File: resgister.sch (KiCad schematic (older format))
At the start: 8 parts, among them U1 74LS245, U2 74LS173, U3 74LS173, U4 74LS245, U5 74LS173, U6 74LS173

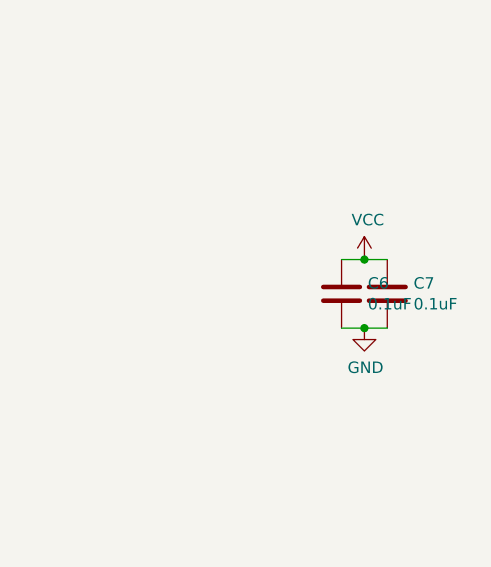
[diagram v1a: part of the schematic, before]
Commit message: added display
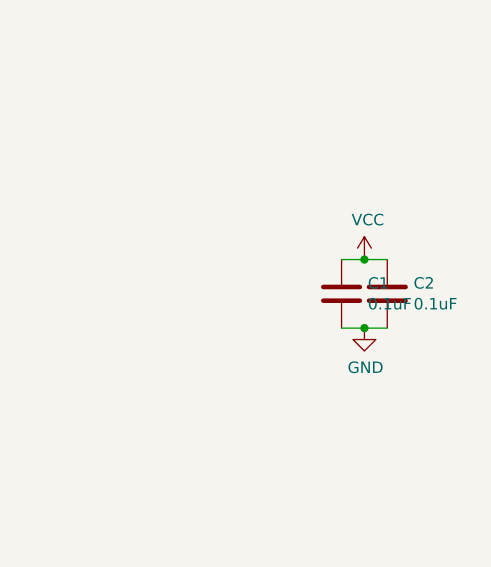
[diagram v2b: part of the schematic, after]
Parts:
- renumbered C8 to C3, C9 to C4

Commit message: clean up
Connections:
- wire segments 281 -> 262
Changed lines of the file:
@@
 $Descr A3 16535 11693
 encoding utf-8
-Sheet 2 23
+Sheet 4 23
 Title ""
 Date ""
@@
 Wire Wire Line
 	3800 4350 3800 1150
-Connection ~ 3800 1150
-Connection ~ 3900 1050
-Connection ~ 4000 950
-Connection ~ 4100 850
-Wire Wire Line
-	3900 1050 9850 1050
-Wire Wire Line
-	3800 1150 9850 1150
-Wire Wire Line
-	4000 950  9850 950
-Wire Wire Line
-	4100 850  9850 850
 Wire Wire Line
 	2000 6100 3250 6100
@@
 Wire Wire Line
 	2700 4100 5250 4100
-Connection ~ 5350 1550
-Connection ~ 5450 1450
-Connection ~ 5550 1350
-Connection ~ 5650 1250
-Wire Wire Line
-	5650 1250 9850 1250
-Wire Wire Line
-	5550 1350 9850 1350
-Wire Wire Line
-	5450 1450 9850 1450
-Wire Wire Line
-	5350 1550 9850 1550
 Wire Wire Line
 	1300 1750 6200 1750
@@
 Wire Wire Line
 	6800 2350 9450 2350
-Connection ~ 7900 1950
-Wire Wire Line
-	7900 1950 9850 1950
-Connection ~ 8000 1850
-Wire Wire Line
-	8000 1850 9850 1850
-Connection ~ 8100 1750
-Wire Wire Line
-	8100 1750 9850 1750
-Connection ~ 8200 1650
-Wire Wire Line
-	8200 1650 9850 1650
-Connection ~ 9450 2350
-Wire Wire Line
-	9450 2350 9850 2350
-Connection ~ 9550 2250
-Wire Wire Line
-	9550 2250 9850 2250
-Connection ~ 9650 2150
-Wire Wire Line
-	9650 2150 9850 2150
-Connection ~ 9750 2050
-Wire Wire Line
-	9750 2050 9850 2050
 Wire Wire Line
 	6100 6900 7500 6900
@@
 AR Path="/5FB94562/61968D37" Ref="#PWR?"  Part="1"
 AR Path="/616D5CDC/61968D37" Ref="#PWR?"  Part="1"
-F 0 "#PWR02" H 2600 4600 50  0001 C CNN
+F 0 "#PWR024" H 2600 4600 50  0001 C CNN
 F 1 "GND" H 2605 4677 50  0000 C CNN
 F 2 "" H 2600 4850 50  0001 C CNN
@@
 AR Path="/5FB94562/61968D38" Ref="#PWR?"  Part="1"
 AR Path="/616D5CDC/61968D38" Ref="#PWR?"  Part="1"
-F 0 "#PWR03" H 3300 3250 50  0001 C CNN
+F 0 "#PWR025" H 3300 3250 50  0001 C CNN
 F 1 "GND" H 3305 3327 50  0000 C CNN
 F 2 "" H 3300 3500 50  0001 C CNN
@@
 AR Path="/5FB94562/61968D39" Ref="#PWR?"  Part="1"
 AR Path="/616D5CDC/61968D39" Ref="#PWR?"  Part="1"
-F 0 "#PWR04" H 4150 3250 50  0001 C CNN
+F 0 "#PWR026" H 4150 3250 50  0001 C CNN
 F 1 "GND" H 4155 3327 50  0000 C CNN
 F 2 "" H 4150 3500 50  0001 C CNN
@@
 AR Path="/5FB94562/5F7355A8" Ref="#PWR?"  Part="1"
 AR Path="/616D5CDC/5F7355A8" Ref="#PWR?"  Part="1"
-F 0 "#PWR07" H 4400 4700 50  0001 C CNN
+F 0 "#PWR029" H 4400 4700 50  0001 C CNN
 F 1 "+5V" H 4415 5023 50  0000 C CNN
 F 2 "" H 4400 4850 50  0001 C CNN
@@
 AR Path="/5FB94562/61968D3C" Ref="#PWR?"  Part="1"
 AR Path="/616D5CDC/61968D3C" Ref="#PWR?"  Part="1"
-F 0 "#PWR09" H 5800 4150 50  0001 C CNN
+F 0 "#PWR031" H 5800 4150 50  0001 C CNN
 F 1 "+5V" H 5815 4473 50  0000 C CNN
 F 2 "" H 5800 4300 50  0001 C CNN
@@
 AR Path="/5FB94562/61968D3D" Ref="#PWR?"  Part="1"
 AR Path="/616D5CDC/61968D3D" Ref="#PWR?"  Part="1"
-F 0 "#PWR017" H 8500 5500 50  0001 C CNN
+F 0 "#PWR039" H 8500 5500 50  0001 C CNN
 F 1 "+5V" H 8515 5823 50  0000 C CNN
 F 2 "" H 8500 5650 50  0001 C CNN
@@
 AR Path="/5FB94562/61968D3E" Ref="#PWR?"  Part="1"
 AR Path="/616D5CDC/61968D3E" Ref="#PWR?"  Part="1"
-F 0 "#PWR018" H 10050 4150 50  0001 C CNN
+F 0 "#PWR040" H 10050 4150 50  0001 C CNN
 F 1 "+5V" H 10065 4473 50  0000 C CNN
 F 2 "" H 10050 4300 50  0001 C CNN
@@
 AR Path="/5FB94562/62492028" Ref="#PWR?"  Part="1"
 AR Path="/616D5CDC/62492028" Ref="#PWR?"  Part="1"
-F 0 "#PWR011" H 5950 3350 50  0001 C CNN
+F 0 "#PWR033" H 5950 3350 50  0001 C CNN
 F 1 "+5V" H 5965 3673 50  0000 C CNN
 F 2 "" H 5950 3500 50  0001 C CNN
@@
 AR Path="/5FB94562/61968D3F" Ref="#PWR?"  Part="1"
 AR Path="/616D5CDC/61968D3F" Ref="#PWR?"  Part="1"
-F 0 "#PWR06" H 4250 2550 50  0001 C CNN
+F 0 "#PWR028" H 4250 2550 50  0001 C CNN
 F 1 "GND" H 4255 2627 50  0000 C CNN
 F 2 "" H 4250 2800 50  0001 C CNN
@@
 Wire Wire Line
 	8750 3800 8750 600
-Connection ~ 8750 600
-Wire Wire Line
-	8750 600  9850 600
 Wire Wire Line
 	4650 3000 4650 600
@@
 	9000 4700 9000 8100
 Connection ~ 7600 4700
-Connection ~ 9000 8100
-Wire Wire Line
-	9000 8100 10200 8100
 Wire Wire Line
 	3000 4000 3000 4050
@@
 Wire Wire Line
 	7100 4800 7100 5300
-Connection ~ 6500 8600
-Wire Wire Line
-	6500 8600 10200 8600
 $Comp
 L 16bitCpu-rescue:74LS173-74xx U?
@@
 AR Path="/5FB94562/5F6AAB55" Ref="U?"  Part="1"
 AR Path="/616D5CDC/5F6AAB55" Ref="U?"  Part="1"
-F 0 "U2" H 3500 5931 50  0000 C CNN
+F 0 "U8" H 3500 5931 50  0000 C CNN
 F 1 "74LS173" H 3500 5840 50  0000 C CNN
 F 2 "Package_DIP:DIP-16_W7.62mm" H 3500 4850 50  0001 C CNN
@@
 AR Path="/5FB94562/5F6AAB61" Ref="U?"  Part="1"
 AR Path="/616D5CDC/5F6AAB61" Ref="U?"  Part="1"
-F 0 "U1" V 2546 2656 50  0000 R CNN
+F 0 "U7" V 2546 2656 50  0000 R CNN
 F 1 "74LS245" V 2455 2656 50  0000 R CNN
 F 2 "Package_DIP:DIP-20_W7.62mm" H 2500 3500 50  0001 C CNN
@@
 AR Path="/5FB94562/616C379E" Ref="U?"  Part="1"
 AR Path="/616D5CDC/616C379E" Ref="U?"  Part="1"
-F 0 "U6" V 9104 5244 50  0000 L CNN
+F 0 "U12" V 9104 5244 50  0000 L CNN
 F 1 "74LS173" V 9195 5244 50  0000 L CNN
 F 2 "Package_DIP:DIP-16_W7.62mm" H 9150 4300 50  0001 C CNN
@@
 AR Path="/5FB94562/61968D34" Ref="#PWR?"  Part="1"
 AR Path="/616D5CDC/61968D34" Ref="#PWR?"  Part="1"
-F 0 "#PWR013" H 7400 4050 50  0001 C CNN
+F 0 "#PWR035" H 7400 4050 50  0001 C CNN
 F 1 "GND" H 7405 4127 50  0000 C CNN
 F 2 "" H 7400 4300 50  0001 C CNN
@@
 AR Path="/5FB94562/616C3790" Ref="#PWR?"  Part="1"
 AR Path="/616D5CDC/616C3790" Ref="#PWR?"  Part="1"
-F 0 "#PWR015" H 8250 4050 50  0001 C CNN
+F 0 "#PWR037" H 8250 4050 50  0001 C CNN
 F 1 "GND" H 8255 4127 50  0000 C CNN
 F 2 "" H 8250 4300 50  0001 C CNN
@@
 AR Path="/5FB94562/616C3791" Ref="#PWR?"  Part="1"
 AR Path="/616D5CDC/616C3791" Ref="#PWR?"  Part="1"
-F 0 "#PWR012" H 6700 5400 50  0001 C CNN
+F 0 "#PWR034" H 6700 5400 50  0001 C CNN
 F 1 "GND" H 6705 5477 50  0000 C CNN
 F 2 "" H 6700 5650 50  0001 C CNN
@@
 AR Path="/5FB94562/62492023" Ref="#PWR?"  Part="1"
 AR Path="/616D5CDC/62492023" Ref="#PWR?"  Part="1"
-F 0 "#PWR05" H 4150 3250 50  0001 C CNN
+F 0 "#PWR027" H 4150 3250 50  0001 C CNN
 F 1 "GND" H 4155 3327 50  0000 C CNN
 F 2 "" H 4150 3500 50  0001 C CNN
@@
 AR Path="/5FB94562/62492019" Ref="#PWR?"  Part="1"
 AR Path="/616D5CDC/62492019" Ref="#PWR?"  Part="1"
-F 0 "#PWR08" H 4400 4700 50  0001 C CNN
+F 0 "#PWR030" H 4400 4700 50  0001 C CNN
 F 1 "+5V" H 4415 5023 50  0000 C CNN
 F 2 "" H 4400 4850 50  0001 C CNN
@@
 AR Path="/5FB94562/6249201A" Ref="#PWR?"  Part="1"
 AR Path="/616D5CDC/6249201A" Ref="#PWR?"  Part="1"
-F 0 "#PWR010" H 5800 4150 50  0001 C CNN
+F 0 "#PWR032" H 5800 4150 50  0001 C CNN
 F 1 "+5V" H 5815 4473 50  0000 C CNN
 F 2 "" H 5800 4300 50  0001 C CNN
@@
 AR Path="/5FB94562/61968D24" Ref="#PWR?"  Part="1"
 AR Path="/616D5CDC/61968D24" Ref="#PWR?"  Part="1"
-F 0 "#PWR016" H 8500 5500 50  0001 C CNN
+F 0 "#PWR038" H 8500 5500 50  0001 C CNN
 F 1 "+5V" H 8515 5823 50  0000 C CNN
 F 2 "" H 8500 5650 50  0001 C CNN
@@
 AR Path="/5FB94562/6249201B" Ref="#PWR?"  Part="1"
 AR Path="/616D5CDC/6249201B" Ref="#PWR?"  Part="1"
-F 0 "#PWR019" H 10050 4150 50  0001 C CNN
+F 0 "#PWR041" H 10050 4150 50  0001 C CNN
 F 1 "+5V" H 10065 4473 50  0000 C CNN
 F 2 "" H 10050 4300 50  0001 C CNN
@@
 AR Path="/5FB94562/616C37AD" Ref="#PWR?"  Part="1"
 AR Path="/616D5CDC/616C37AD" Ref="#PWR?"  Part="1"
-F 0 "#PWR014" H 7800 3400 50  0001 C CNN
+F 0 "#PWR036" H 7800 3400 50  0001 C CNN
 F 1 "GND" H 7805 3477 50  0000 C CNN
 F 2 "" H 7800 3650 50  0001 C CNN
@@
 AR Path="/5FB94562/61968D33" Ref="U?"  Part="1"
 AR Path="/616D5CDC/61968D33" Ref="U?"  Part="1"
-F 0 "U5" V 7554 6594 50  0000 L CNN
+F 0 "U11" V 7554 6594 50  0000 L CNN
 F 1 "74LS173" V 7645 6594 50  0000 L CNN
 F 2 "Package_DIP:DIP-16_W7.62mm" H 7600 5650 50  0001 C CNN
@@
 AR Path="/5FB94562/5F73559C" Ref="U?"  Part="1"
 AR Path="/616D5CDC/5F73559C" Ref="U?"  Part="1"
-F 0 "U3" V 5004 4444 50  0000 L CNN
+F 0 "U9" V 5004 4444 50  0000 L CNN
 F 1 "74LS173" V 5095 4444 50  0000 L CNN
 F 2 "Package_DIP:DIP-16_W7.62mm" H 5050 3500 50  0001 C CNN
@@
 AR Path="/5FB94562/62492020" Ref="U?"  Part="1"
 AR Path="/616D5CDC/62492020" Ref="U?"  Part="1"
-F 0 "U4" V 6646 3456 50  0000 R CNN
+F 0 "U10" V 6646 3456 50  0000 R CNN
 F 1 "74LS245" V 6555 3456 50  0000 R CNN
 F 2 "Package_DIP:DIP-20_W7.62mm" H 6600 4300 50  0001 C CNN
@@
 AR Path="/5FB94562/61968D30" Ref="#PWR?"  Part="1"
 AR Path="/616D5CDC/61968D30" Ref="#PWR?"  Part="1"
-F 0 "#PWR01" H 1700 3350 50  0001 C CNN
+F 0 "#PWR023" H 1700 3350 50  0001 C CNN
 F 1 "+5V" H 1715 3673 50  0000 C CNN
 F 2 "" H 1700 3500 50  0001 C CNN
@@
 AR Path="/5F74778C/5FB15BC2" Ref="#PWR042"  Part="1"
 AR Path="/5F67C726/5FB15BC2" Ref="#PWR020"  Part="1"
-F 0 "#PWR020" H 11950 2250 50  0001 C CNN
+F 0 "#PWR042" H 11950 2250 50  0001 C CNN
 F 1 "VCC" H 11965 2573 50  0000 C CNN
 F 2 "" H 11950 2400 50  0001 C CNN
@@
 AR Path="/5F74778C/5FB15BC8" Ref="#PWR043"  Part="1"
 AR Path="/5F67C726/5FB15BC8" Ref="#PWR021"  Part="1"
-F 0 "#PWR021" H 11950 2450 50  0001 C CNN
+F 0 "#PWR043" H 11950 2450 50  0001 C CNN
 F 1 "GND" H 11955 2527 50  0000 C CNN
 F 2 "" H 11950 2700 50  0001 C CNN
@@
 AR Path="/5F74778C/5FB15BD0" Ref="C3"  Part="1"
 AR Path="/5F67C726/5FB15BD0" Ref="C1"  Part="1"
-F 0 "C1" H 11965 2596 50  0000 L CNN
+F 0 "C3" H 11965 2596 50  0000 L CNN
 F 1 "0.1uF" H 11965 2505 50  0000 L CNN
 F 2 "Capacitor_THT:CP_Axial_L10.0mm_D4.5mm_P15.00mm_Horizontal" H 11888 2400 50  0001 C CNN
@@
 AR Path="/5F74778C/5FB15BDA" Ref="C4"  Part="1"
 AR Path="/5F67C726/5FB15BDA" Ref="C2"  Part="1"
-F 0 "C2" H 12165 2596 50  0000 L CNN
+F 0 "C4" H 12165 2596 50  0000 L CNN
 F 1 "0.1uF" H 12165 2505 50  0000 L CNN
 F 2 "Capacitor_THT:CP_Axial_L10.0mm_D4.5mm_P15.00mm_Horizontal" H 12088 2400 50  0001 C CNN
